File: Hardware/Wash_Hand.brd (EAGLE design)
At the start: 71.1 x 48.3 mm, 91 parts, among them IC1 LM358D, IC2 LP298XS, IC3 405016TSSOP, J1 I2C, J2 ICSP, J3 SPI, J4 9V_CONN, J5 EXT_VCC, J6 6_PIN_SERIAL_CABLEPTH, J7 OP_B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

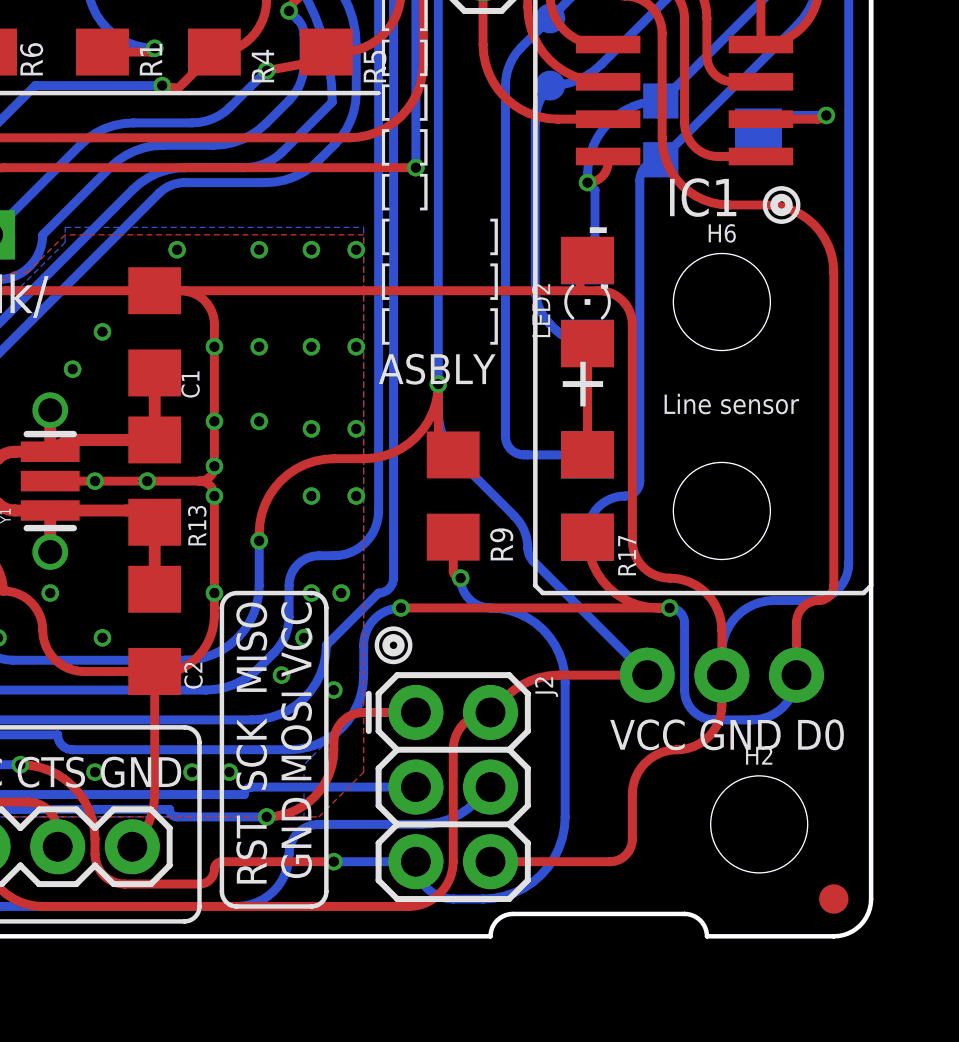
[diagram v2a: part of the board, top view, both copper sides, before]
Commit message: Board/Schematic: Route Orange LED2 to NPN_COLLECTOR
instead of the common ground. This way when we disable
the ON_OFF_SWT the light will not be light up.

Signed-off-by: Konrad Rzeszutek Wilk <konrad@kernel.org>
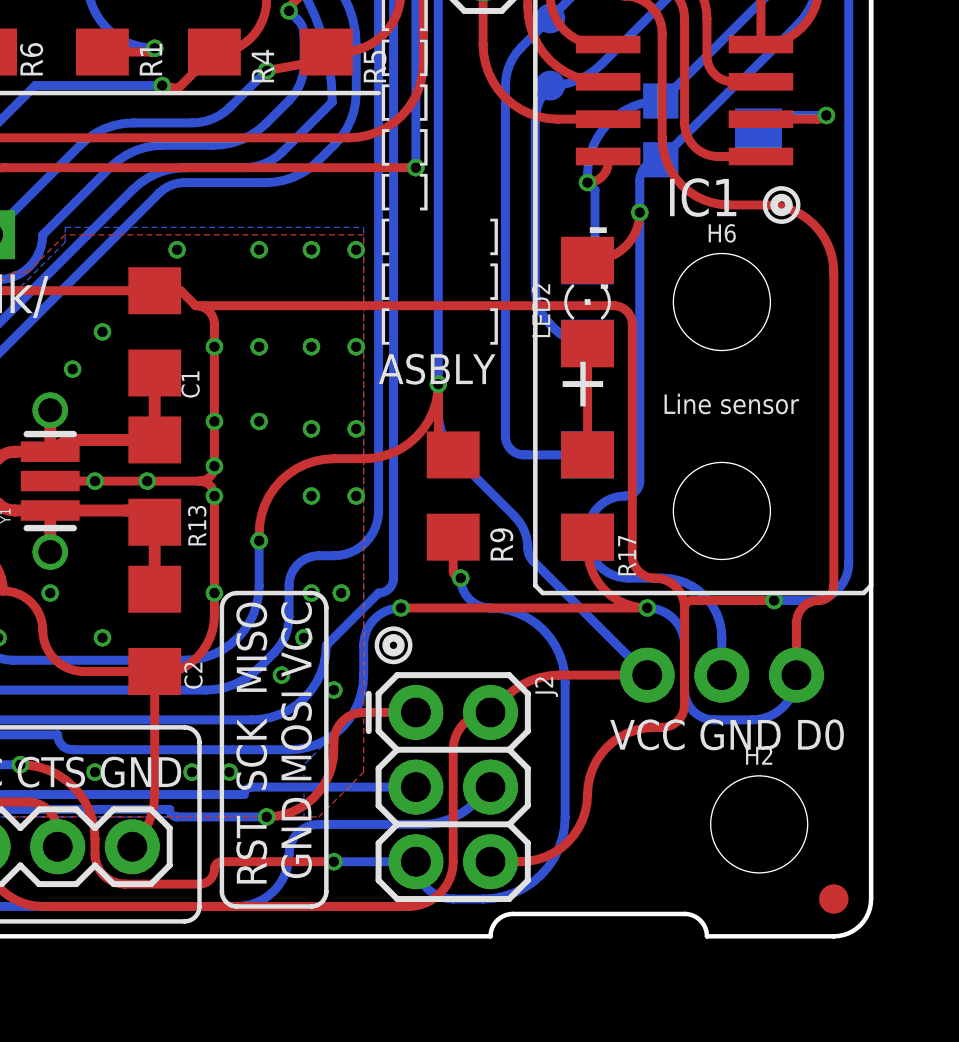
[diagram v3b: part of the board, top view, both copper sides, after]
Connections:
- net 0: no longer J.2, LED2.C
- net NPN_COLLECTOR: now also J.2, LED2.C
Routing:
- net NPN_COLLECTOR: track 41.9 -> 51.7 mm, vias 1 -> 2
- net 0: track 375.0 -> 370.3 mm, vias 112 -> 113
- net D0: track 105.6 -> 104.6 mm
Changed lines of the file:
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@@
 <wire x1="48.768" y1="11.684" x2="48.768" y2="10.922" width="0.3048" layer="1"/>
 <wire x1="46.736" y1="21.974" x2="47.622" y2="21.974" width="0.3048" layer="1"/>
-<wire x1="47.622" y1="21.974" x2="48.768" y2="20.828" width="0.3048" layer="1" curve="-90"/>
+<wire x1="47.622" y1="21.974" x2="48.13" y2="21.466" width="0.3048" layer="1"/>
+<wire x1="48.13" y1="21.466" x2="48.768" y2="20.828" width="0.3048" layer="1" curve="-90"/>
 <wire x1="48.768" y1="20.828" x2="48.768" y2="20.066" width="0.3048" layer="1"/>
 <wire x1="48.768" y1="20.066" x2="48.768" y2="17.526" width="0.3048" layer="1"/>
@@
 <wire x1="20.32" y1="39.878" x2="19.304" y2="39.878" width="0.3048" layer="16"/>
 <wire x1="19.304" y1="39.878" x2="18.034" y2="39.878" width="0.3048" layer="16"/>
-<wire x1="47.622" y1="21.974" x2="61.214" y2="21.974" width="0.3048" layer="1"/>
-<wire x1="61.214" y1="21.974" x2="61.846" y2="21.974" width="0.3048" layer="1"/>
-<wire x1="62.992" y1="13.462" x2="64.262" y2="12.192" width="0.3048" layer="1" curve="90"/>
-<wire x1="64.262" y1="12.192" x2="66.04" y2="10.414" width="0.3048" layer="1" curve="-90"/>
-<wire x1="62.992" y1="13.462" x2="62.992" y2="20.828" width="0.3048" layer="1"/>
+<wire x1="48.13" y1="21.466" x2="62.354" y2="21.466" width="0.3048" layer="1"/>
 <wire x1="62.738" y1="45.974" x2="60.96" y2="44.196" width="0.3048" layer="16" curve="-90"/>
 <wire x1="60.96" y1="44.196" x2="55.118" y2="44.196" width="0.3048" layer="16"/>
@@
 <wire x1="47.752" y1="44.196" x2="49.276" y2="45.72" width="0.3048" layer="1" curve="90"/>
 <wire x1="49.276" y1="45.72" x2="49.276" y2="45.7501" width="0.3048" layer="1"/>
-<wire x1="58.166" y1="2.54" x2="62.23" y2="2.54" width="0.3048" layer="1"/>
-<wire x1="62.992" y1="4.826" x2="64.516" y2="6.35" width="0.3048" layer="1" curve="-90"/>
-<wire x1="62.992" y1="3.302" x2="62.23" y2="2.54" width="0.3048" layer="1" curve="-90"/>
-<wire x1="62.992" y1="4.826" x2="62.992" y2="3.302" width="0.3048" layer="1"/>
 <via x="48.768" y="17.526" extent="1-16" drill="0.35"/>
 <via x="48.768" y="11.684" extent="1-16" drill="0.35"/>
@@
 <via x="13.462" y="5.842" extent="1-16" drill="0.35"/>
 <contactref element="LED1" pad="A"/>
-<wire x1="62.992" y1="20.828" x2="61.846" y2="21.974" width="0.3048" layer="1" curve="90"/>
+<wire x1="62.354" y1="21.466" x2="62.992" y2="20.828" width="0.3048" layer="1" curve="-90"/>
 <contactref element="U1" pad="1"/>
 <contactref element="C12" pad="1"/>
@@
 <via x="4.318" y="24.13" extent="1-16" drill="0.35"/>
 <contactref element="T1" pad="2"/>
-<contactref element="LED2" pad="C"/>
-<contactref element="J" pad="2"/>
-<wire x1="66.04" y1="10.414" x2="66.04" y2="8.89" width="0.3048" layer="1"/>
-<wire x1="64.516" y1="6.35" x2="66.04" y2="7.874" width="0.3048" layer="1" curve="90"/>
-<wire x1="66.04" y1="7.874" x2="66.04" y2="8.89" width="0.3048" layer="1"/>
 <wire x1="62.738" y1="45.974" x2="62.738" y2="40.64" width="0.3048" layer="16"/>
 <via x="62.738" y="40.64" extent="1-16" drill="0.35"/>
 <wire x1="62.738" y1="40.64" x2="63.8302" y2="40.64" width="0.3048" layer="1"/>
 <wire x1="63.8302" y1="40.64" x2="64.0842" y2="40.386" width="0.3048" layer="1" curve="-90"/>
-<wire x1="61.214" y1="21.974" x2="61.214" y2="22.758" width="0.3048" layer="1"/>
-<wire x1="61.214" y1="22.758" x2="61.468" y2="23.012" width="0.3048" layer="1" curve="-90"/>
 <via x="35.56" y="21.082" extent="1-16" drill="0.35"/>
 <wire x1="62.738" y1="40.64" x2="68.072" y2="40.64" width="0.3048" layer="16"/>
 <wire x1="68.072" y1="40.64" x2="69.596" y2="40.64" width="0.3048" layer="16"/>
 <wire x1="70.358" y1="39.878" x2="69.596" y2="40.64" width="0.3048" layer="16" curve="90"/>
-<wire x1="66.04" y1="8.89" x2="66.04" y2="9.652" width="0.3048" layer="16"/>
-<wire x1="66.04" y1="9.652" x2="67.818" y2="11.43" width="0.3048" layer="16" curve="-90"/>
 <wire x1="67.818" y1="11.43" x2="69.088" y2="11.43" width="0.3048" layer="16"/>
 <wire x1="69.088" y1="11.43" x2="70.358" y2="12.7" width="0.3048" layer="16" curve="90"/>
@@
 <contactref element="JP7" pad="1"/>
 <wire x1="68.072" y1="39.7764" x2="68.072" y2="40.64" width="0.3048" layer="16"/>
+<wire x1="62.992" y1="12.954" x2="63.754" y2="12.192" width="0.3048" layer="1" curve="90"/>
+<wire x1="64.77" y1="11.176" x2="63.754" y2="12.192" width="0.3048" layer="1" curve="90"/>
+<wire x1="64.77" y1="7.874" x2="64.008" y2="7.112" width="0.3048" layer="1" curve="-90"/>
+<wire x1="64.008" y1="7.112" x2="63.754" y2="7.112" width="0.3048" layer="1"/>
+<wire x1="63.754" y1="7.112" x2="61.468" y2="4.826" width="0.3048" layer="1" curve="90"/>
+<wire x1="61.468" y1="4.826" x2="59.182" y2="2.54" width="0.3048" layer="1" curve="-90"/>
+<wire x1="59.182" y1="2.54" x2="58.166" y2="2.54" width="0.3048" layer="1"/>
+<wire x1="62.992" y1="20.828" x2="62.992" y2="12.954" width="0.3048" layer="1"/>
+<wire x1="64.77" y1="11.176" x2="64.77" y2="7.874" width="0.3048" layer="1"/>
+<via x="67.818" y="11.43" extent="1-16" drill="0.35"/>
+<wire x1="67.818" y1="11.43" x2="65.024" y2="11.43" width="0.3048" layer="1"/>
+<wire x1="65.024" y1="11.43" x2="64.77" y2="11.176" width="0.3048" layer="1" curve="90"/>
 </signal>
 <signal name="D0">
@@
 <wire x1="67.056" y1="7.366" x2="65.786" y2="7.366" width="0.3048" layer="16"/>
 <wire x1="65.786" y1="7.366" x2="64.77" y2="8.382" width="0.3048" layer="16" curve="-90"/>
-<wire x1="64.77" y1="8.382" x2="64.77" y2="10.668" width="0.3048" layer="16"/>
-<wire x1="64.77" y1="10.668" x2="64.262" y2="11.176" width="0.3048" layer="16" curve="90"/>
-<via x="64.262" y="11.176" extent="1-16" drill="0.35"/>
-<wire x1="64.262" y1="11.176" x2="55.118" y2="11.176" width="0.3048" layer="1"/>
+<wire x1="64.77" y1="8.382" x2="64.77" y2="9.906" width="0.3048" layer="16"/>
+<wire x1="64.77" y1="9.906" x2="63.5" y2="11.176" width="0.3048" layer="16" curve="90"/>
+<via x="63.5" y="11.176" extent="1-16" drill="0.35"/>
+<wire x1="63.5" y1="11.176" x2="55.118" y2="11.176" width="0.3048" layer="1"/>
 <via x="55.118" y="11.176" extent="1-16" drill="0.35"/>
 <wire x1="55.118" y1="11.176" x2="53.848" y2="9.906" width="0.3048" layer="16" curve="90"/>
@@
 <wire x1="62.1284" y1="39.37" x2="61.3156" y2="39.37" width="0.3048" layer="1"/>
 <contactref element="R17" pad="1"/>
-<wire x1="61.468" y1="13.586" x2="63.878" y2="11.176" width="0.3048" layer="1" curve="90"/>
-<wire x1="63.878" y1="11.176" x2="64.262" y2="11.176" width="0.3048" layer="1"/>
 <wire x1="67.564" y1="24.892" x2="66.294" y2="24.892" width="0.3048" layer="1"/>
 <wire x1="66.294" y1="24.892" x2="64.008" y2="27.178" width="0.3048" layer="1" curve="-90"/>
@@
 <wire x1="62.23" y1="36.068" x2="62.484" y2="35.814" width="0.3048" layer="1" curve="-90"/>
 <wire x1="62.484" y1="35.814" x2="62.484" y2="33.528" width="0.3048" layer="1"/>
+<wire x1="61.468" y1="13.586" x2="61.468" y2="13.208" width="0.3048" layer="1"/>
+<wire x1="61.468" y1="13.208" x2="63.5" y2="11.176" width="0.3048" layer="1" curve="90"/>
 </signal>
 <signal name="SDA">
@@
 <wire x1="62.738" y1="14.986" x2="63.246" y2="15.494" width="0.3048" layer="16" curve="90"/>
 <wire x1="63.246" y1="25.717" x2="63.961" y2="26.432" width="0.3048" layer="16" curve="-90"/>
-<wire x1="63.246" y1="15.494" x2="63.246" y2="25.717" width="0.3048" layer="16"/>
+<wire x1="63.246" y1="15.494" x2="63.246" y2="24.638" width="0.3048" layer="16"/>
 <contactref element="JP7" pad="2"/>
+<wire x1="63.246" y1="24.638" x2="63.246" y2="25.717" width="0.3048" layer="16"/>
 <wire x1="68.072" y1="38.9636" x2="66.3956" y2="38.9636" width="0.3048" layer="16"/>
 <wire x1="66.3956" y1="38.9636" x2="65.024" y2="37.592" width="0.3048" layer="16" curve="90"/>
@@
 <wire x1="65.024" y1="37.338" x2="65.0494" y2="37.3126" width="0.3048" layer="1" curve="-90"/>
 <wire x1="65.0494" y1="37.3126" x2="65.0494" y2="34.2646" width="0.3048" layer="1"/>
+<contactref element="LED2" pad="C"/>
+<contactref element="J" pad="2"/>
+<wire x1="61.468" y1="23.012" x2="61.62" y2="23.012" width="0.3048" layer="1"/>
+<wire x1="61.62" y1="23.012" x2="63.246" y2="24.638" width="0.3048" layer="1" curve="90"/>
+<via x="63.246" y="24.638" extent="1-16" drill="0.35"/>
+<wire x1="61.468" y1="13.586" x2="62.862" y2="12.192" width="0.3048" layer="16" curve="90"/>
+<wire x1="62.862" y1="12.192" x2="64.008" y2="12.192" width="0.3048" layer="16"/>
+<wire x1="64.008" y1="12.192" x2="66.04" y2="10.16" width="0.3048" layer="16" curve="-90"/>
+<wire x1="66.04" y1="10.16" x2="66.04" y2="8.89" width="0.3048" layer="16"/>
 </signal>
 <signal name="N$16">

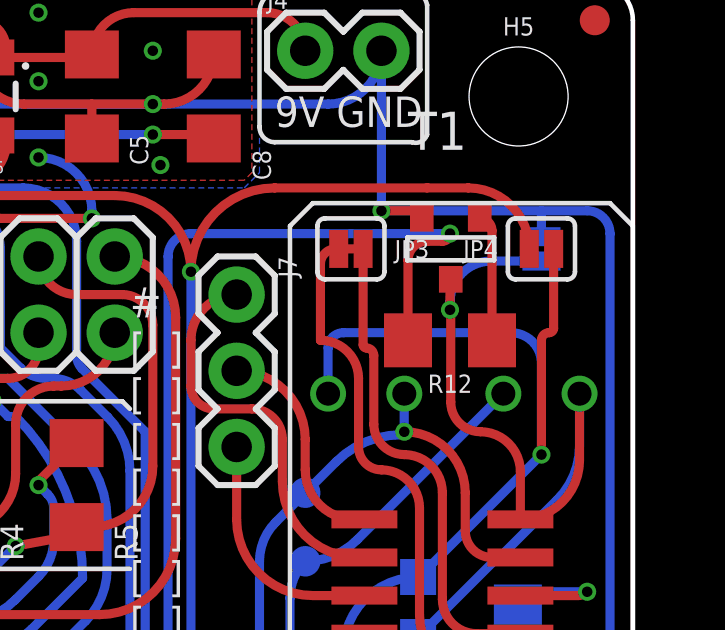
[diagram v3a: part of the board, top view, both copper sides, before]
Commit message: Schematic: Move R12 up just a bit.
Signed-off-by: Konrad Rzeszutek Wilk <konrad@kernel.org>
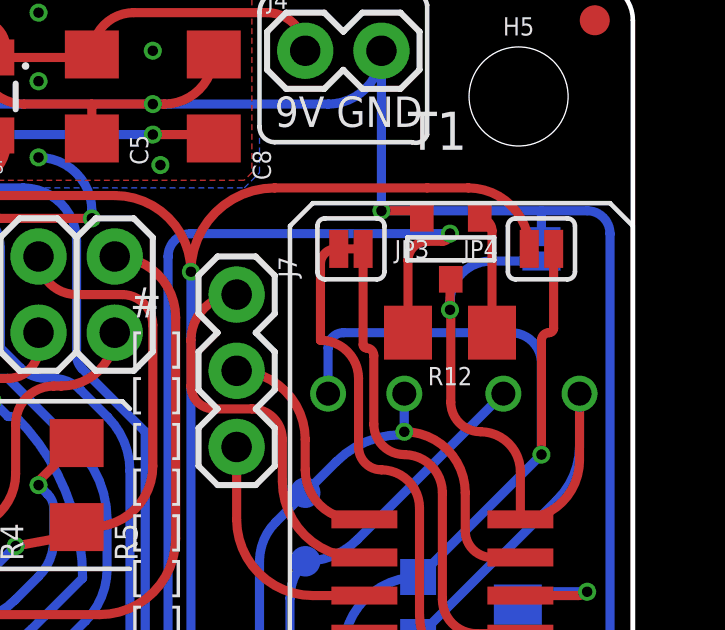
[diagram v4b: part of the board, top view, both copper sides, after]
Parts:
- moved R12 0.25 mm to (65.0, 36.6)
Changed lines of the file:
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@@
 <attribute name="VALUE" x="39.878" y="34.163" size="0.6096" layer="27" font="vector" ratio="20"/>
 </element>
-<element name="R12" library="darnok_common" package="1206" value="1.2K" x="65.024" y="36.322" smashed="yes" rot="R180">
-<attribute name="NAME" x="65.024" y="35.179" size="0.6096" layer="25" font="vector" ratio="20" rot="R180" align="bottom-center"/>
-<attribute name="VALUE" x="65.024" y="37.465" size="0.6096" layer="27" font="vector" ratio="20" rot="R180" align="top-center"/>
+<element name="R12" library="darnok_common" package="1206" value="1.2K" x="65.024" y="36.576" smashed="yes" rot="R180">
+<attribute name="NAME" x="65.024" y="35.433" size="0.6096" layer="25" font="vector" ratio="20" rot="R180" align="bottom-center"/>
+<attribute name="VALUE" x="65.024" y="37.719" size="0.6096" layer="27" font="vector" ratio="20" rot="R180" align="top-center"/>
 </element>
 <element name="LOGO2" library="darnok_logo" package="HAPPY_FACE_LOGO" value="HAPPY_FACE_LOGO" x="33.528" y="44.196" smashed="yes" rot="MR0"/>
@@
 <wire x1="64.77" y1="39.624" x2="64.262" y2="39.624" width="0.3048" layer="1"/>
 <wire x1="64.262" y1="39.624" x2="63.624" y2="38.986" width="0.3048" layer="1" curve="90"/>
-<wire x1="63.624" y1="38.986" x2="63.624" y2="36.322" width="0.3048" layer="1"/>
+<wire x1="63.624" y1="38.986" x2="63.624" y2="36.576" width="0.3048" layer="1"/>
 </signal>
 <signal name="N$15">
@@
 <contactref element="T1" pad="3"/>
 <contactref element="R12" pad="1"/>
-<wire x1="66.424" y1="36.322" x2="66.424" y2="39.9766" width="0.3048" layer="1"/>
+<wire x1="66.424" y1="36.576" x2="66.424" y2="39.9766" width="0.3048" layer="1"/>
 <wire x1="66.424" y1="39.9766" x2="66.0146" y2="40.386" width="0.3048" layer="1" curve="90"/>
 </signal>

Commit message: Board/Schematic: Add values and move text around a bit
so that it is not over the board.

Signed-off-by: Konrad Rzeszutek Wilk <konrad@kernel.org>
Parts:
- T1: value NPN -> MMBT3904
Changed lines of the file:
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@@
 <element name="JP4" library="SparkFun-Jumpers" library_urn="urn:adsk.eagle:library:528" package="SMT-JUMPER_2_NC_PASTE_SILK" package3d_urn="urn:adsk.eagle:package:39282/1" value="ENA_INT_SENSOR" x="68.072" y="39.37" smashed="yes">
 <attribute name="NAME" x="66.04" y="39.0525" size="0.6096" layer="25" font="vector" ratio="20" align="bottom-center"/>
-<attribute name="VALUE" x="68.072" y="37.4015" size="0.6096" layer="27" font="vector" ratio="20" align="top-center"/>
+<attribute name="VALUE" x="67.564" y="36.3855" size="0.6096" layer="27" font="vector" ratio="20" align="top-center"/>
 </element>
 <element name="R15" library="darnok_common" package="1206" value="10K" x="61.468" y="14.986" smashed="yes" rot="MR90">
@@
 <element name="LED2" library="adafruit" library_urn="urn:adsk.eagle:library:420" package="1206" package3d_urn="urn:adsk.eagle:package:6240349/1" value="ORANGE" x="61.468" y="21.59" smashed="yes" rot="R90">
 <attribute name="NAME" x="60.198" y="20.32" size="0.6096" layer="25" rot="R90"/>
-<attribute name="VALUE" x="64.008" y="20.32" size="1.27" layer="27" rot="R90"/>
+<attribute name="VALUE" x="64.008" y="20.32" size="0.635" layer="27" ratio="15" rot="R90"/>
 </element>
 <element name="R18" library="darnok_common" package="1206" value="100K" x="25.908" y="31.496" smashed="yes" rot="R90">
@@
 <attribute name="VALUE" x="55.88" y="39.116" size="0.6096" layer="27" font="vector" ratio="20" rot="R270"/>
 </element>
-<element name="T1" library="zetex" library_urn="urn:adsk.eagle:library:418" package="SOT-23" package3d_urn="urn:adsk.eagle:package:30981/1" value="NPN" x="65.024" y="39.37" smashed="yes">
+<element name="T1" library="zetex" library_urn="urn:adsk.eagle:library:418" package="SOT-23" package3d_urn="urn:adsk.eagle:package:30981/1" value="MMBT3904" x="65.024" y="39.37" smashed="yes">
 <attribute name="MF" value="" x="65.024" y="39.37" size="1.778" layer="27" display="off"/>
 <attribute name="MPN" value="DSS20201L-7" x="65.024" y="39.37" size="1.778" layer="27" display="off"/>
@@
 <attribute name="OC_NEWARK" value="25R4555" x="65.024" y="39.37" size="1.778" layer="27" display="off"/>
 <attribute name="POPULARITY" value="0" x="65.024" y="39.37" size="1.778" layer="27" display="off"/>
-<attribute name="VALUE" x="63.627" y="41.148" size="1.27" layer="27" ratio="10"/>
+<attribute name="VALUE" x="63.119" y="41.148" size="0.635" layer="27" ratio="25"/>
 </element>
 <element name="J8" library="SparkFun-Connectors" library_urn="urn:adsk.eagle:library:513" package="2X6" package3d_urn="urn:adsk.eagle:package:38277/1" value="2X6 FEMALE" x="41.148" y="36.576" smashed="yes">

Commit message: RELEASE-1.4-rc5
Signed-off-by: Konrad Rzeszutek Wilk <konrad@kernel.org>
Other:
- board text added: "v1.4-rc5"
- board text removed: "v1.4-rc4"
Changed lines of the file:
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@@
 <circle x="8.636" y="38.862" radius="0.254" width="0.254" layer="25"/>
 <circle x="8.636" y="38.862" radius="0.567959375" width="0.1524" layer="25"/>
-<text x="33.02" y="5.842" size="1.778" layer="26" ratio="14" rot="MR0">v1.4-rc4</text>
+<text x="33.02" y="5.842" size="1.778" layer="26" ratio="14" rot="MR0">v1.4-rc5</text>
 <text x="54.356" y="18.796" size="1.016" layer="25" ratio="14">#
 [  ]
